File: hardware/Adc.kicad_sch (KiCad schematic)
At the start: 36 parts

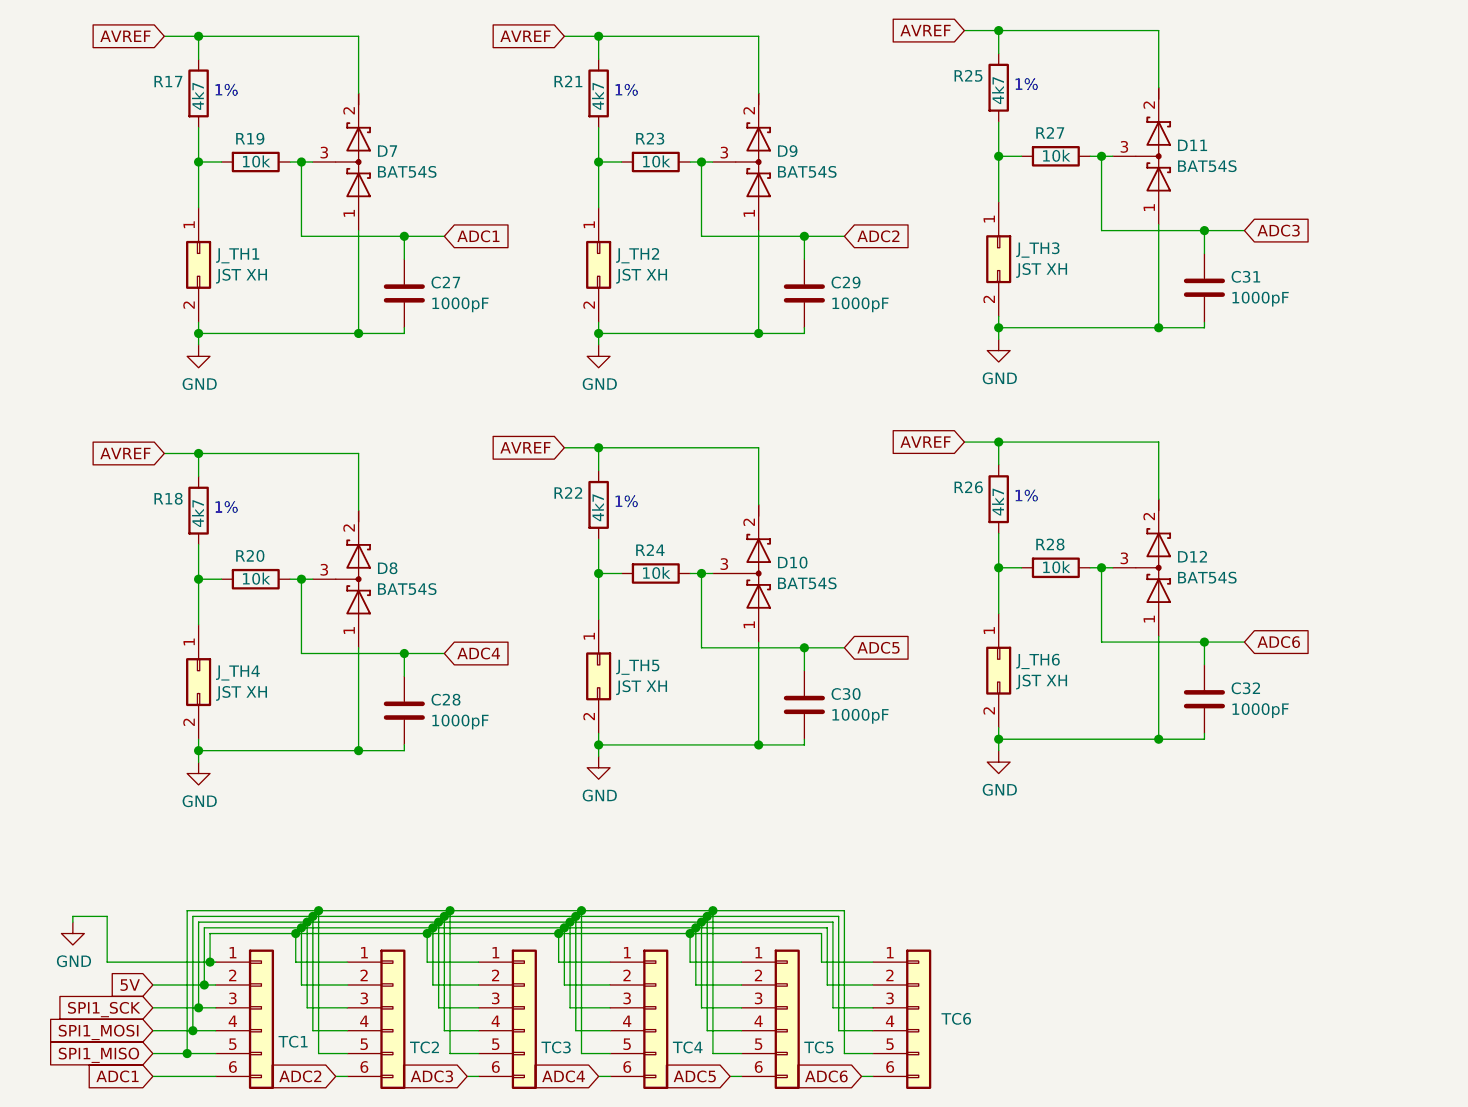
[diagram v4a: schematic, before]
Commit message: Improve ADC ground: add separate GNDA bus; add ferrite bead to AVREF power.
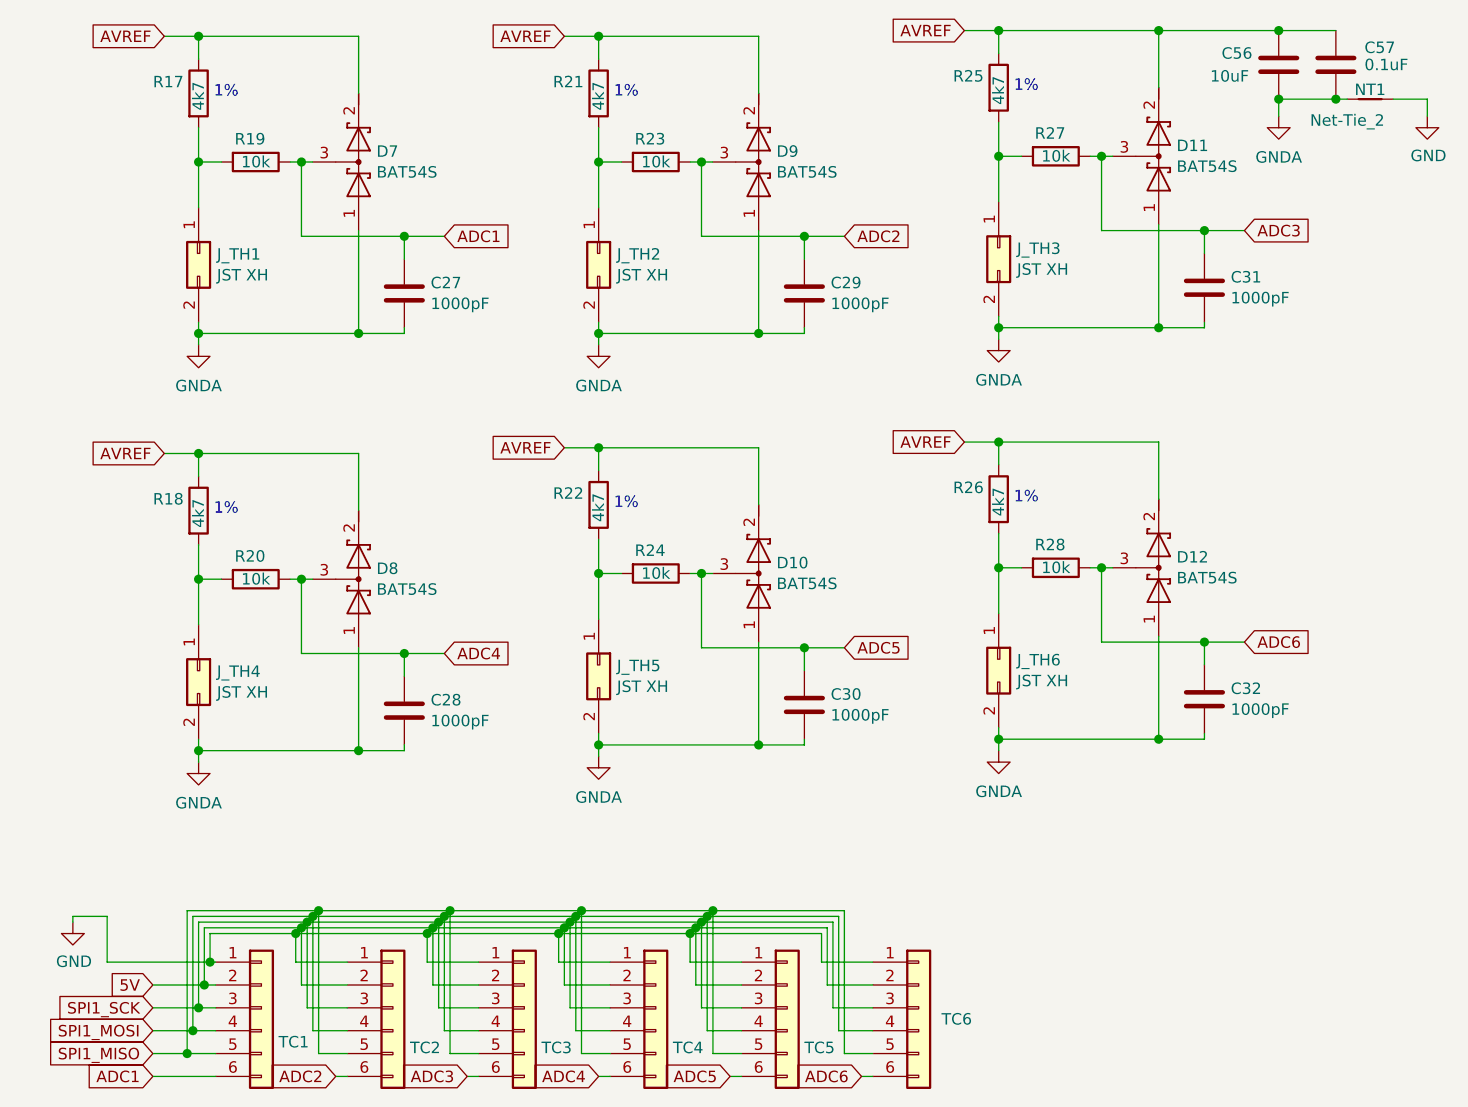
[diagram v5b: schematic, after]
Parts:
- added C56: 10uF, PrntrBoardV2:C_0603_1608Metric, symbol Device:C
- added C57: 0.1uF, PrntrBoardV2:C_0603_1608Metric, symbol Device:C
- added NT1: Net-Tie_2, NetTie:NetTie-2_SMD_Pad0.5mm, symbol Device:Net-Tie_2
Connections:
- net AVREF: now also C56.1, C57.1
- net GND: now also NT1.2; no longer C27.2, C28.2, C29.2, C30.2, C31.2, C32.2, D10.1 (A), D11.1 (A), D12.1 (A), D7.1 (A), D8.1 (A), D9.1 (A), J_TH1.2 (Pin_2), J_TH2.2 (Pin_2), J_TH3.2 (Pin_2), J_TH4.2 (Pin_2), J_TH5.2 (Pin_2), J_TH6.2 (Pin_2)
- new net GNDA: C27.2, C28.2, C29.2, C30.2, C31.2, C32.2, C56.2, C57.2, D10.1 (A), D11.1 (A), D12.1 (A), D7.1 (A), D8.1 (A), D9.1 (A), J_TH1.2 (Pin_2), J_TH2.2 (Pin_2), J_TH3.2 (Pin_2), J_TH4.2 (Pin_2), J_TH5.2 (Pin_2), J_TH6.2 (Pin_2), NT1.1
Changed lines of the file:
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@@
   (junction (at 133.985 34.925) (diameter 1.016) (color 0 0 0 0))
   (junction (at 133.985 80.645) (diameter 1.016) (color 0 0 0 0))
+  (junction (at 140.335 20.955) (diameter 1.016) (color 0 0 0 0))
   (junction (at 140.335 53.975) (diameter 1.016) (color 0 0 0 0))
   (junction (at 140.335 99.695) (diameter 1.016) (color 0 0 0 0))
   (junction (at 145.415 43.18) (diameter 1.016) (color 0 0 0 0))
   (junction (at 145.415 88.9) (diameter 1.016) (color 0 0 0 0))
+  (junction (at 153.67 20.955) (diameter 1.016) (color 0 0 0 0))
+  (junction (at 153.67 28.575) (diameter 1.016) (color 0 0 0 0))
+  (junction (at 160.02 28.575) (diameter 1.016) (color 0 0 0 0))
   (wire (pts (xy 19.685 119.38) (xy 19.685 120.015))
     (stroke (width 0) (type solid) (color 0 0 0 0))
@@
     (stroke (width 0) (type solid) (color 0 0 0 0))
   )
+  (wire (pts (xy 140.335 20.955) (xy 153.67 20.955))
+    (stroke (width 0) (type solid) (color 0 0 0 0))
+  )
   (wire (pts (xy 140.335 27.305) (xy 140.335 20.955))
     (stroke (width 0) (type solid) (color 0 0 0 0))
@@
   )
   (wire (pts (xy 145.415 99.695) (xy 140.335 99.695))
+    (stroke (width 0) (type solid) (color 0 0 0 0))
+  )
+  (wire (pts (xy 153.67 20.955) (xy 160.02 20.955))
+    (stroke (width 0) (type solid) (color 0 0 0 0))
+  )
+  (wire (pts (xy 153.67 28.575) (xy 153.67 30.48))
+    (stroke (width 0) (type solid) (color 0 0 0 0))
+  )
+  (wire (pts (xy 160.02 28.575) (xy 153.67 28.575))
+    (stroke (width 0) (type solid) (color 0 0 0 0))
+  )
+  (wire (pts (xy 160.02 28.575) (xy 161.29 28.575))
+    (stroke (width 0) (type solid) (color 0 0 0 0))
+  )
+  (wire (pts (xy 170.18 28.575) (xy 166.37 28.575))
+    (stroke (width 0) (type solid) (color 0 0 0 0))
+  )
+  (wire (pts (xy 170.18 30.48) (xy 170.18 28.575))
     (stroke (width 0) (type solid) (color 0 0 0 0))
   )
@@
     )
   )
+  (symbol (lib_id "Device:Net-Tie_2") (at 163.83 28.575 0) (unit 1)
+    (in_bom yes) (on_board yes)
+    (property "Reference" "NT1" (id 0) (at 163.83 27.5294 0))
+    (property "Value" "Net-Tie_2" (id 1) (at 161.29 30.9395 0))
+    (property "Footprint" "NetTie:NetTie-2_SMD_Pad0.5mm" (id 2) (at 163.83 28.575 0)
+      (effects (font (size 1.27 1.27)) hide)
+    )
+    (property "Datasheet" "~" (id 3) (at 163.83 28.575 0)
+      (effects (font (size 1.27 1.27)) hide)
+    )
+    (pin "1")
+    (pin "2")
+  )
   (symbol (lib_id "power:GND") (at 19.685 120.015 0) (unit 1)
     (in_bom yes) (on_board yes)
@@
     (pin "1")
   )
-  (symbol (lib_id "power:GND") (at 33.655 55.88 0) (unit 1)
-    (in_bom yes) (on_board yes)
+  (symbol (lib_id "power:GNDA") (at 33.655 55.88 0) (unit 1)
+    (in_bom yes) (on_board yes) (fields_autoplaced)
     (property "Reference" "#PWR022" (id 0) (at 33.655 62.23 0)
       (effects (font (size 1.27 1.27)) hide)
     )
-    (property "Value" "GND" (id 1) (at 33.782 60.2742 0))
+    (property "Value" "GNDA" (id 1) (at 33.655 60.4426 0))
     (property "Footprint" "" (id 2) (at 33.655 55.88 0)
       (effects (font (size 1.27 1.27)) hide)
@@
     (pin "1")
   )
-  (symbol (lib_id "power:GND") (at 33.655 102.235 0) (unit 1)
-    (in_bom yes) (on_board yes)
+  (symbol (lib_id "power:GNDA") (at 33.655 102.235 0) (unit 1)
+    (in_bom yes) (on_board yes) (fields_autoplaced)
     (property "Reference" "#PWR023" (id 0) (at 33.655 108.585 0)
       (effects (font (size 1.27 1.27)) hide)
     )
-    (property "Value" "GND" (id 1) (at 33.782 106.6292 0))
+    (property "Value" "GNDA" (id 1) (at 33.655 106.7976 0))
     (property "Footprint" "" (id 2) (at 33.655 102.235 0)
       (effects (font (size 1.27 1.27)) hide)
@@
     (pin "1")
   )
-  (symbol (lib_id "power:GND") (at 78.105 55.88 0) (unit 1)
-    (in_bom yes) (on_board yes)
+  (symbol (lib_id "power:GNDA") (at 78.105 55.88 0) (unit 1)
+    (in_bom yes) (on_board yes) (fields_autoplaced)
     (property "Reference" "#PWR024" (id 0) (at 78.105 62.23 0)
       (effects (font (size 1.27 1.27)) hide)
     )
-    (property "Value" "GND" (id 1) (at 78.232 60.2742 0))
+    (property "Value" "GNDA" (id 1) (at 78.105 60.4426 0))
     (property "Footprint" "" (id 2) (at 78.105 55.88 0)
       (effects (font (size 1.27 1.27)) hide)
@@
     (pin "1")
   )
-  (symbol (lib_id "power:GND") (at 78.105 101.6 0) (unit 1)
-    (in_bom yes) (on_board yes)
+  (symbol (lib_id "power:GNDA") (at 78.105 101.6 0) (unit 1)
+    (in_bom yes) (on_board yes) (fields_autoplaced)
     (property "Reference" "#PWR025" (id 0) (at 78.105 107.95 0)
       (effects (font (size 1.27 1.27)) hide)
     )
-    (property "Value" "GND" (id 1) (at 78.232 105.9942 0))
+    (property "Value" "GNDA" (id 1) (at 78.105 106.1626 0))
     (property "Footprint" "" (id 2) (at 78.105 101.6 0)
       (effects (font (size 1.27 1.27)) hide)
@@
     (pin "1")
   )
-  (symbol (lib_id "power:GND") (at 122.555 55.245 0) (unit 1)
-    (in_bom yes) (on_board yes)
+  (symbol (lib_id "power:GNDA") (at 122.555 55.245 0) (unit 1)
+    (in_bom yes) (on_board yes) (fields_autoplaced)
     (property "Reference" "#PWR026" (id 0) (at 122.555 61.595 0)
       (effects (font (size 1.27 1.27)) hide)
     )
-    (property "Value" "GND" (id 1) (at 122.682 59.6392 0))
+    (property "Value" "GNDA" (id 1) (at 122.555 59.8076 0))
     (property "Footprint" "" (id 2) (at 122.555 55.245 0)
       (effects (font (size 1.27 1.27)) hide)
@@
     (pin "1")
   )
-  (symbol (lib_id "power:GND") (at 122.555 100.965 0) (unit 1)
-    (in_bom yes) (on_board yes)
+  (symbol (lib_id "power:GNDA") (at 122.555 100.965 0) (unit 1)
+    (in_bom yes) (on_board yes) (fields_autoplaced)
     (property "Reference" "#PWR027" (id 0) (at 122.555 107.315 0)
       (effects (font (size 1.27 1.27)) hide)
     )
-    (property "Value" "GND" (id 1) (at 122.682 105.3592 0))
+    (property "Value" "GNDA" (id 1) (at 122.555 105.5276 0))
     (property "Footprint" "" (id 2) (at 122.555 100.965 0)
       (effects (font (size 1.27 1.27)) hide)
     )
     (property "Datasheet" "" (id 3) (at 122.555 100.965 0)
+      (effects (font (size 1.27 1.27)) hide)
+    )
+    (pin "1")
+  )
+  (symbol (lib_id "power:GNDA") (at 153.67 30.48 0) (unit 1)
+    (in_bom yes) (on_board yes) (fields_autoplaced)
+    (property "Reference" "#PWR076" (id 0) (at 153.67 36.83 0)
+      (effects (font (size 1.27 1.27)) hide)
+    )
+    (property "Value" "GNDA" (id 1) (at 153.67 35.0426 0))
+    (property "Footprint" "" (id 2) (at 153.67 30.48 0)
+      (effects (font (size 1.27 1.27)) hide)
+    )
+    (property "Datasheet" "" (id 3) (at 153.67 30.48 0)
+      (effects (font (size 1.27 1.27)) hide)
+    )
+    (pin "1")
+  )
+  (symbol (lib_id "power:GND") (at 170.18 30.48 0) (unit 1)
+    (in_bom yes) (on_board yes)
+    (property "Reference" "#PWR077" (id 0) (at 170.18 36.83 0)
+      (effects (font (size 1.27 1.27)) hide)
+    )
+    (property "Value" "GND" (id 1) (at 170.307 34.8742 0))
+    (property "Footprint" "" (id 2) (at 170.18 30.48 0)
+      (effects (font (size 1.27 1.27)) hide)
+    )
+    (property "Datasheet" "" (id 3) (at 170.18 30.48 0)
       (effects (font (size 1.27 1.27)) hide)
     )
@@
       (effects (font (size 1.27 1.27)) hide)
     )
+    (pin "1")
+    (pin "2")
+  )
+  (symbol (lib_id "Device:C") (at 153.67 24.765 0) (unit 1)
+    (in_bom yes) (on_board yes)
+    (property "Reference" "C56" (id 0) (at 147.32 23.495 0)
+      (effects (font (size 1.27 1.27)) (justify left))
+    )
+    (property "Value" "10uF" (id 1) (at 146.05 26.035 0)
+      (effects (font (size 1.27 1.27)) (justify left))
+    )
+    (property "Footprint" "PrntrBoardV2:C_0603_1608Metric" (id 2) (at 154.6352 28.575 0)
+      (effects (font (size 1.27 1.27)) hide)
+    )
+    (property "Datasheet" "~" (id 3) (at 153.67 24.765 0)
+      (effects (font (size 1.27 1.27)) hide)
+    )
+    (property "Part #" "CL10A106KP8NNNC" (id 4) (at 153.67 24.765 0)
+      (effects (font (size 1.27 1.27)) hide)
+    )
+    (property "LCSC Part #" "C19702" (id 5) (at 153.67 24.765 0)
+      (effects (font (size 1.27 1.27)) hide)
+    )
+    (pin "1")
+    (pin "2")
+  )
+  (symbol (lib_id "Device:C") (at 160.02 24.765 0) (unit 1)
+    (in_bom yes) (on_board yes)
+    (property "Reference" "C57" (id 0) (at 163.195 22.86 0)
+      (effects (font (size 1.27 1.27)) (justify left))
+    )
+    (property "Value" "0.1uF" (id 1) (at 163.195 24.765 0)
+      (effects (font (size 1.27 1.27)) (justify left))
+    )
+    (property "Footprint" "PrntrBoardV2:C_0603_1608Metric" (id 2) (at 160.9852 28.575 0)
+      (effects (font (size 1.27 1.27)) hide)
+    )
+    (property "Datasheet" "~" (id 3) (at 160.02 24.765 0)
+      (effects (font (size 1.27 1.27)) hide)
+    )
+    (property "Part #" "CC0603KRX7R9BB104" (id 4) (at 160.02 24.765 0)
+      (effects (font (size 1.27 1.27)) hide)
+    )
+    (property "LCSC Part #" "C14663" (id 5) (at 160.02 24.765 0)
+      (effects (font (size 1.27 1.27)) hide)
+    )
